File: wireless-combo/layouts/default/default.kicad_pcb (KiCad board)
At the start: 2 copper layers, 50 x 40 mm, 30 parts

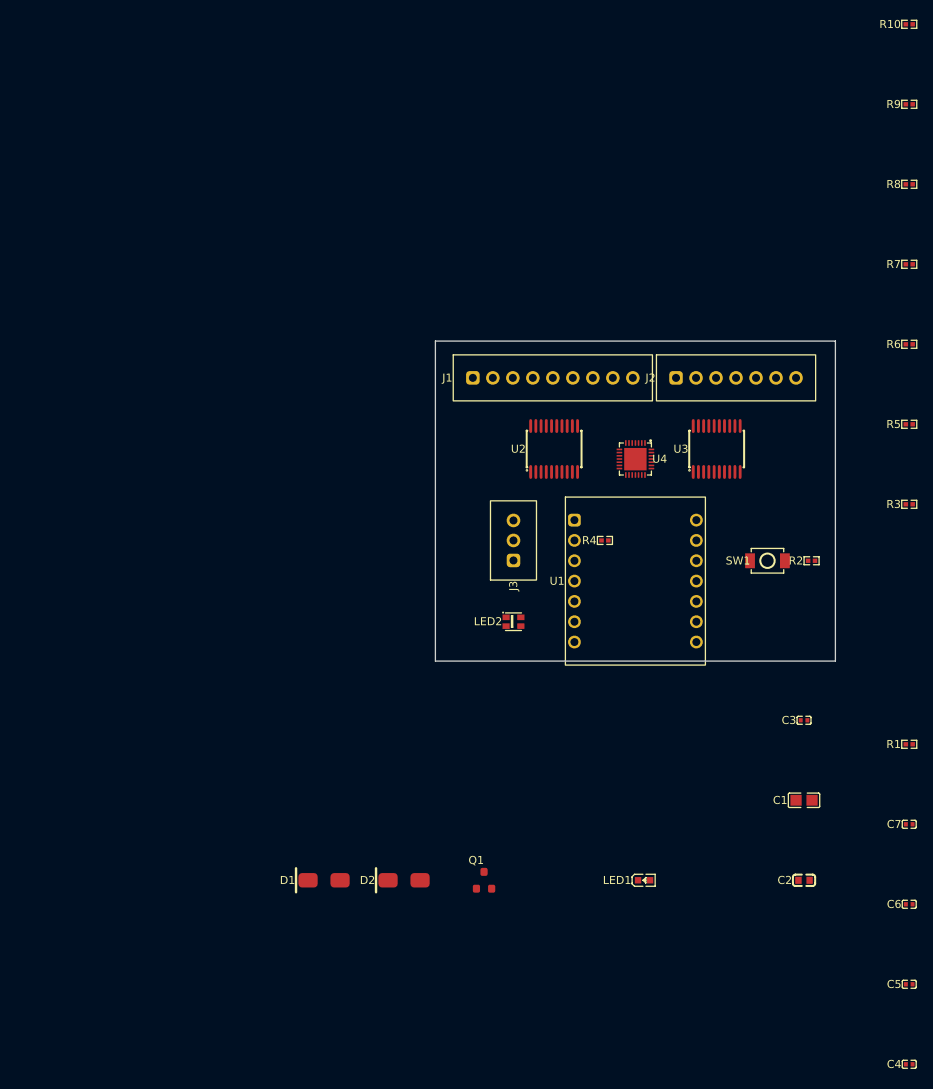
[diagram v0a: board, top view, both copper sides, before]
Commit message: wireless-combo: J1/J2 をボックスヘッダ化、M3 ネジ穴 ×4 追加、4 層化
- J1 (ジョイスティック) を JST XH 9P → 2x5 ボックスヘッダ (LCSC C5665) に変更。
  IDC 圧着型 D-SUB 9pin をそのまま付けたフラットケーブルが使える
  AT/Intel 配列 (ヘッダ 1,2,3.. = D-SUB 1,6,2,7,3,8,4,9,5)。余り Pin10 は GND
- J2 (キーボード) を JST XH 7P → 2x4 ボックスヘッダ (LCSC C9135) に変更。
  ヘッダ Pin n = DIN Pin n、余り Pin8 は GND
- M3 メッキ穴 (MountingHole_3.2mm_M3_Pad_Via) を H1-H4 として追加し GND に接続。
  BOM / CPL からは除外
- 基板を 4 層 (atari-joystick-slim と同じスタックアップ、総厚 1.6mm) に変更
- フットプリント / 3D モデルは KiCad 標準ライブラリのコピー。NOTICE に追記
- 不要になった parts/JST_XH_B9B, JST_XH_B7B を削除
- レイアウトは作業途中 (部品配置・ゾーン追加中、未配線)

Co-Authored-By: Claude Opus 5.5 <noreply@anthropic.com>
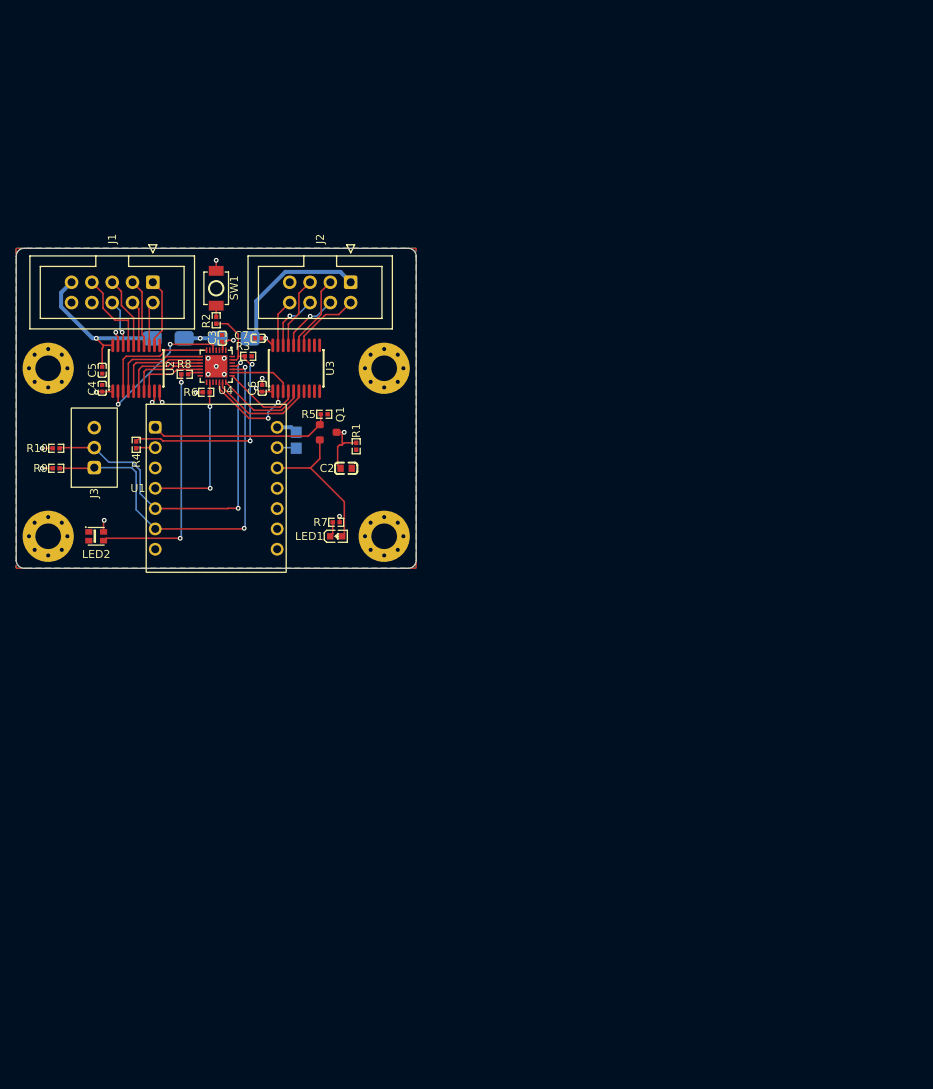
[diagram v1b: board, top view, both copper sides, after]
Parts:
- added H1: , MountingHole_M3:MountingHole_M3, F.Cu at (79.0, 75.0)
- added H2: , MountingHole_M3:MountingHole_M3, F.Cu at (121.0, 75.0)
- added H3: , MountingHole_M3:MountingHole_M3, F.Cu at (121.0, 96.0)
- added H4: , MountingHole_M3:MountingHole_M3, F.Cu at (79.0, 96.0)
- C1, D1, D2: moved to B.Cu
- J1: footprint JST_XH_B9B:JST_XH_B9B -> IDC_Header_2x05:IDC_Header_2x05
- J2: footprint JST_XH_B7B:JST_XH_B7B -> IDC_Header_2x04:IDC_Header_2x04
- moved C4 131.6 mm to (85.8, 77.5), turned to 90 degrees
- moved C5 126.8 mm to (85.8, 75.2), turned to -90 degrees
- moved R10 119.1 mm to (80.0, 85.0)
- moved R9 115.9 mm to (80.0, 87.5)
- moved C6 103.4 mm to (105.8, 77.5), turned to 90 degrees
- moved C7 101.6 mm to (105.2, 71.2), turned to 180 degrees
- moved R8 93.6 mm to (96.1, 75.8), turned to 180 degrees
- moved R6 88.1 mm to (98.8, 78.0)
- moved C3 87.0 mm to (100.8, 71.2), turned to 90 degrees
- moved R3 84.7 mm to (104.0, 73.5)
- moved R2 80.3 mm to (100.0, 69.0), turned to -90 degrees
- moved R7 78.6 mm to (115.0, 94.2)
- moved R1 78.5 mm to (117.5, 84.8), turned to -90 degrees
- moved C1 77.8 mm to (110.0, 84.0), turned to -90 degrees
- moved C2 77.0 mm to (116.2, 87.5)
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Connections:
- J1 pad 2: down -> triga
- J1 pad 3: left -> down
- J1 pad 4: right -> trigb
- J1 pad 5: VCC_JOY -> left
- J1 pad 6: triga -> common
- J1 pad 7: trigb -> right
- J1 pad 8: common -> GND
- J1 pad 9: GND -> VCC_JOY
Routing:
- net SCL_SWCLK: track 0.00 -> 51.0 mm, vias 0 -> 2
- net SDA_SWDIO: track 0.00 -> 46.8 mm, vias 0 -> 2
- net usb_dp: track 0.00 -> 33.6 mm, vias 0 -> 2
- net din: track 0.00 -> 30.3 mm, vias 0 -> 2
- net VCC_ESP: track 0.00 -> 24.8 mm, vias 0 -> 1
- net CH32_PWR_OFF: track 0.00 -> 23.0 mm
- net VDD_SW: track 0.00 -> 22.0 mm, vias 0 -> 9
- net VCC_JOY: track 0.00 -> 21.8 mm, vias 0 -> 1
- net VCC_KBD: track 0.00 -> 21.7 mm, vias 0 -> 1
- net CH32_INT: track 0.00 -> 20.1 mm, vias 0 -> 2
- net VDD33: track 0.00 -> 18.6 mm
- net COMMON_3V3: track 0.00 -> 17.9 mm, vias 0 -> 2
- net RIGHT_3V3: track 0.00 -> 14.9 mm
- net GND: track 0.00 -> 14.7 mm, vias 0 -> 10
- net MSDATA_3V3: track 0.00 -> 13.1 mm
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- added copper zone on B.Cu, net GND
- added copper zone on F.Cu, net GND
- added copper zone on In1.Cu, net GND
- added copper zone on In2.Cu, net VDD_SW
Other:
- outline, holes or cut-outs redrawn
- copper layers 2 -> 4

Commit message: wireless-combo: レイアウトの配線を完了 (4 層, DRC クリーン)
部品配置・GND/VDD_SW ゾーン・配線を完了。KiCad DRC は違反 0 / 未配線 0。
README の状態表記を「未配線」から「配線済み・未発注」に更新。

Co-Authored-By: Claude Opus 5.5 <noreply@anthropic.com>
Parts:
- moved J1 10.4 mm to (81.9, 66.3), turned to 90 degrees
- moved J2 7.88 mm to (109.2, 66.3), turned to 90 degrees
- moved D1 6.76 mm to (98.0, 65.8), turned to 90 degrees
- moved D2 5.51 mm to (102.0, 65.8), turned to 90 degrees
- moved C2 4.21 mm to (112.2, 86.2), turned to -90 degrees
- moved R1 3.93 mm to (113.8, 85.9)
- moved Q1 2.20 mm to (111.8, 83.0)
- moved R5 2.20 mm to (111.3, 80.7)
- moved R8 1.00 mm to (96.0, 76.8)
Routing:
- net triga: track 5.53 -> 18.9 mm
- net trigb: track 5.67 -> 12.3 mm, vias 0 -> 1
- net remote: track 7.23 -> 13.2 mm, vias 1 -> 2
- net VCC_KBD: track 21.7 -> 16.2 mm, vias 1 -> 0
- net up: track 8.75 -> 13.9 mm, vias 0 -> 1
- net right: track 10.7 -> 6.09 mm
- net GND: track 14.7 -> 10.8 mm, vias 10 -> 11
- net VCC_ESP: track 24.8 -> 28.0 mm
- net common: track 5.91 -> 8.98 mm, vias 1 -> 0
- net key_rxd: track 9.51 -> 6.44 mm
- net msdata: track 8.72 -> 11.6 mm, vias 0 -> 2
- net VDD_SW: track 22.0 -> 19.2 mm
- net VCC_JOY: track 21.8 -> 24.2 mm
- net CH32_PWR_OFF: track 23.0 -> 20.8 mm
- net down: track 8.48 -> 10.5 mm, vias 0 -> 1
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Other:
- board text added: "BOOT"
- board text added: "Mimic X Combo"
- board text added: "PWR"
- board text added: "STAT"
- board text added: "v1.0.0 Developed by @kunichiko"

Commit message: wireless-combo: タイトル / リビジョンを設定し、v1.0.0 製造データを生成
- 3 基板の KiCad title_block に TITLE / REVISION (v1.0.0) を設定し、
  シルクの版数表記を ${REVISION} 参照に変更
    default  = MimicX-combo
    joystick = MimicX-breakout-atari-joystick
    keyboard = MimicX-breakout-x68000-keyboard
- Fabrication Toolkit の ARCHIVE_NAME を ${TITLE}_${REVISION} にして
  production/ (Gerber zip / BOM / CPL / netlist) を生成
- default: solder_mask_to_copper_clearance 0.005
- keyboard: J2 (Mini DIN) のリファレンス表示を非表示

Co-Authored-By: Claude Opus 5.5 <noreply@anthropic.com>
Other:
- board text added: "${REVISION} Developed by @kunichiko"
- board text removed: "v1.0.0 Developed by @kunichiko"
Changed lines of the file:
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@@
 	)
 	(paper "A4")
+	(title_block
+		(title "MimicX-combo")
+		(rev "v1.0.0")
+	)
 	(layers
 		(0 "F.Cu" signal)
@@
 		)
 	)
-	(gr_text "v1.0.0 Developed by @kunichiko"
+	(gr_text "${REVISION} Developed by @kunichiko"
 		(at 117.75 85.5 270)
 		(layer "F.SilkS")
